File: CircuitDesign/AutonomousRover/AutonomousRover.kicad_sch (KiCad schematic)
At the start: 15 parts

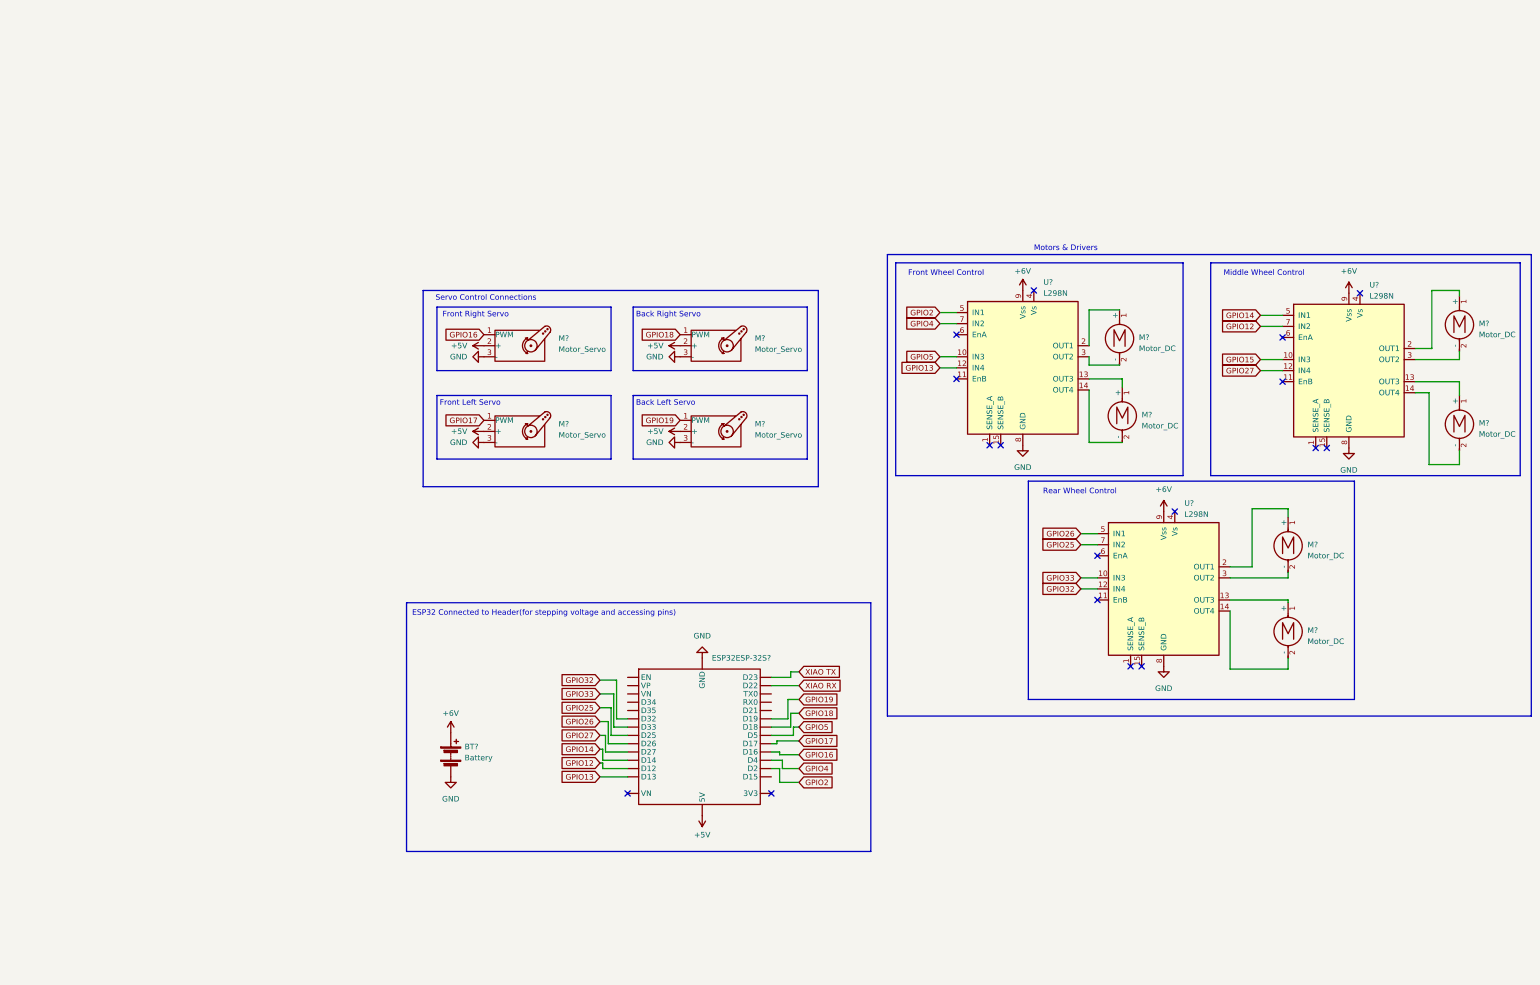
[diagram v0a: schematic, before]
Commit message: CAD, brief update, and circuit update
- Trailer CAD final
- Camera Holder CAD
- Brief update
- Circuit schematic update
- Fixed turning
- Log reasoning for full_stop from camera
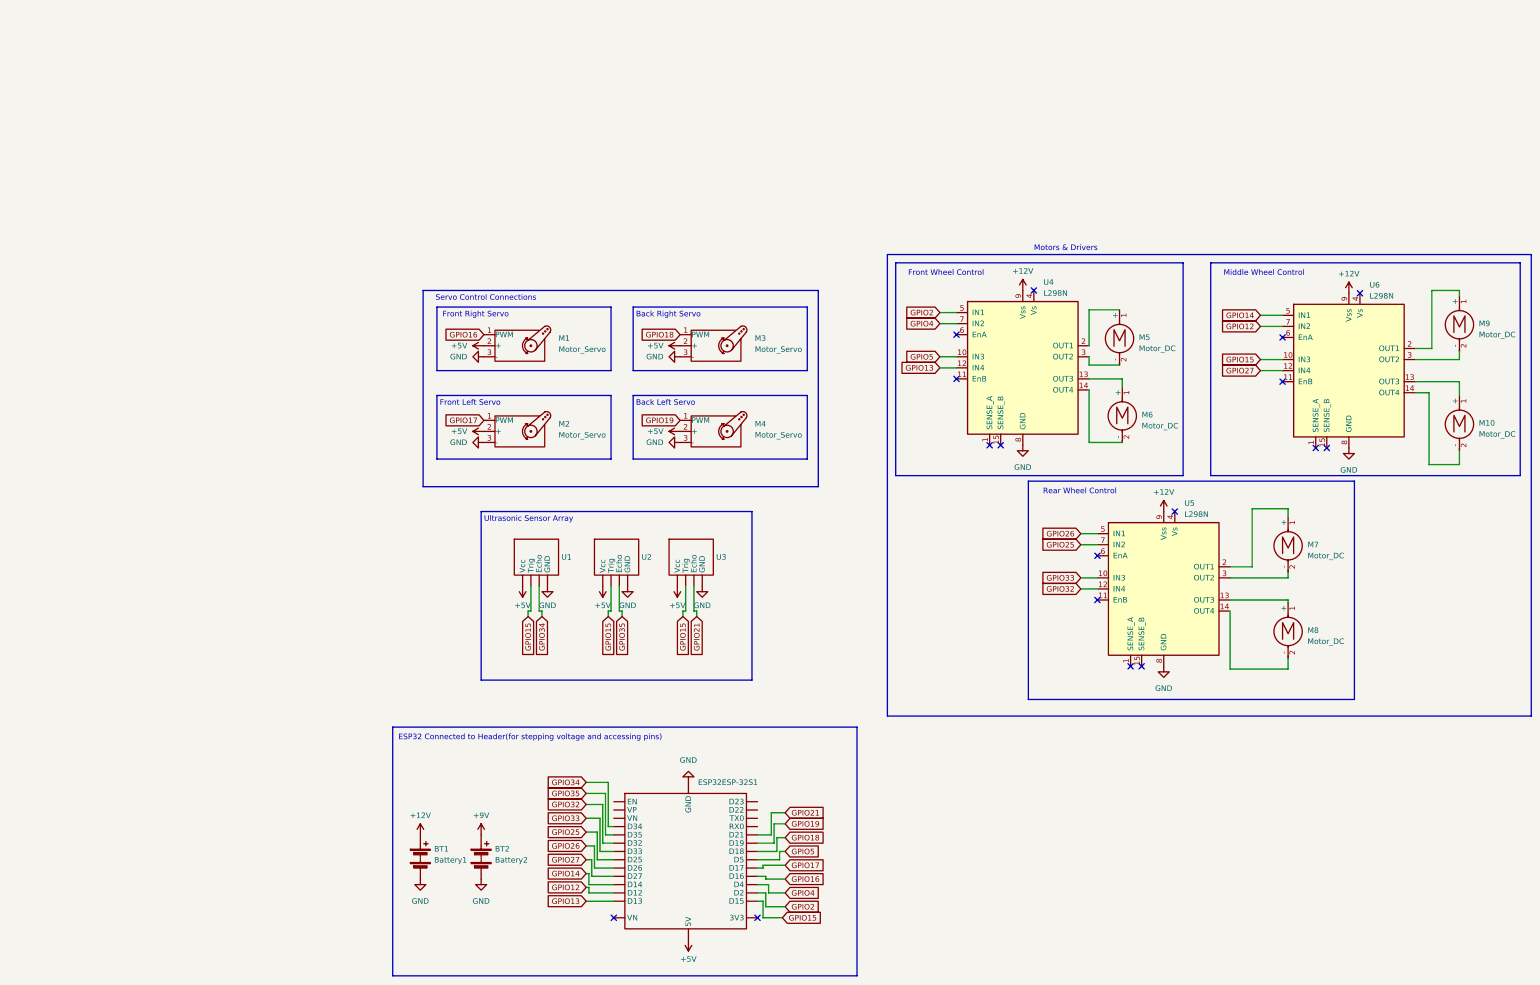
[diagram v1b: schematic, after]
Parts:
- added BT2: Battery2, symbol Device:Battery
- added U1, U2, U3: ~, symbol CustomSymbols:HC-SR04
- BT1: renamed from BT?; value Battery -> Battery1
- gave numbers to parts that had none: 14
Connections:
- net XIAO RX is gone; now on net GPIO5: ESP32ESP-32S1. (VP)
- net XIAO TX is gone; now on net GPIO5: ESP32ESP-32S1. (VP)
- net +5V: now also U1. (Vcc), U2. (Vcc), U3. (Vcc)
- net GND: now also BT2.2 (-), U1. (Vcc), U2. (Vcc), U3. (Vcc)
- net GPIO15: now also ESP32ESP-32S1. (VP), U1. (Vcc), U2. (Vcc), U3. (Vcc)
- net +6V renamed +12V
- new net +9V: BT2.1 (+)
- new net GPIO21: ESP32ESP-32S1. (VP), U3. (Vcc)
- new net GPIO34: ESP32ESP-32S1. (VP), U1. (Vcc)
- new net GPIO35: ESP32ESP-32S1. (VP), U2. (Vcc)
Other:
- note added: "Ultrasonic Sensor Array"
- moved on the sheet: BT1, ESP32ESP-32S1

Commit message: Updates to controller, server, and rover driver code
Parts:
- removed U2, U3: ~, symbol CustomSymbols:HC-SR04
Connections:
- net GPIO21 is gone; now on net GPIO5: ESP32ESP-32S1. (VP)
- net GPIO35 is gone; now on net GPIO5: ESP32ESP-32S1. (VP)
- no-connect marks 17 -> 28
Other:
- note added: "Ultrasonic Sensor"
- note removed: "Ultrasonic Sensor Array"

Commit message: Updated wiring and started TOF integration
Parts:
- removed U1: ~, symbol CustomSymbols:HC-SR04
- added VL53L5CX1: ~, symbol CustomSymbols:VL53L5CX
- renumbered U4 to U1, U5 to U2, U6 to U3
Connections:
- net GPIO34 is gone; now on net GPIO5: ESP32ESP-32S1. (VP)
- net GND: now also VL53L5CX1. (VIN)
- new net +3.3V: ESP32ESP-32S1. (VP), VL53L5CX1. (VIN)
- new net GPIO21: ESP32ESP-32S1. (VP), VL53L5CX1. (VIN)
- new net GPIO22: ESP32ESP-32S1. (VP), VL53L5CX1. (VIN)
- no-connect marks 28 -> 26
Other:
- note added: "TOF Sensor"
- note removed: "Ultrasonic Sensor"

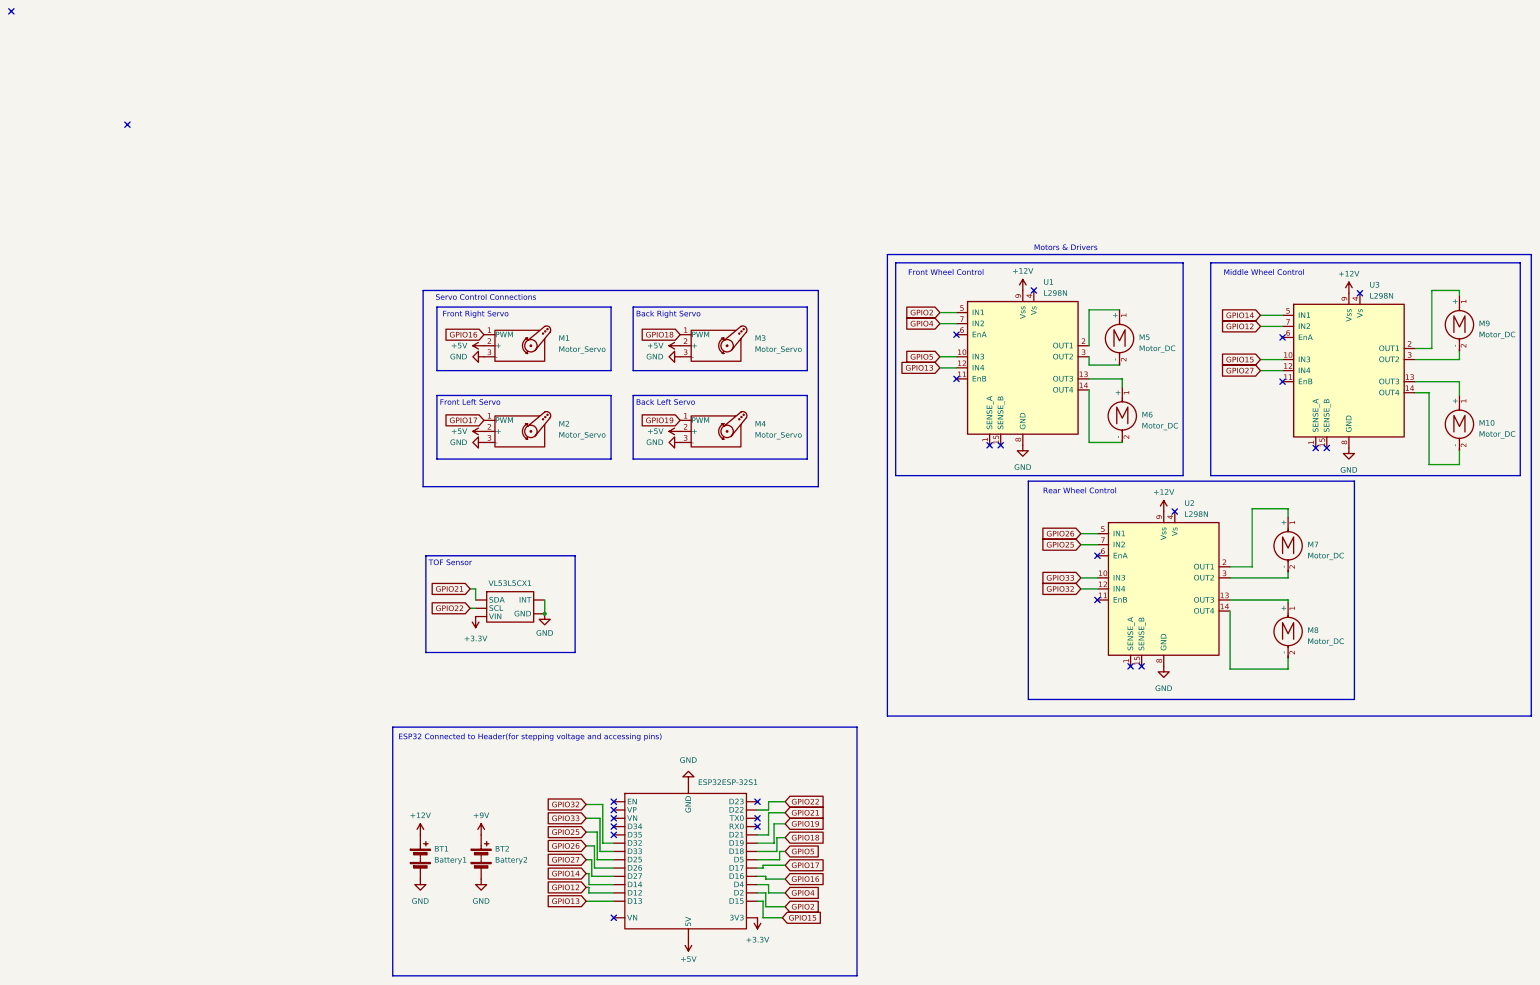
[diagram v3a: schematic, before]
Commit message: Directory clean up, removed servo, US Sensor. and middle motor code, and TOF sensor integration with OD
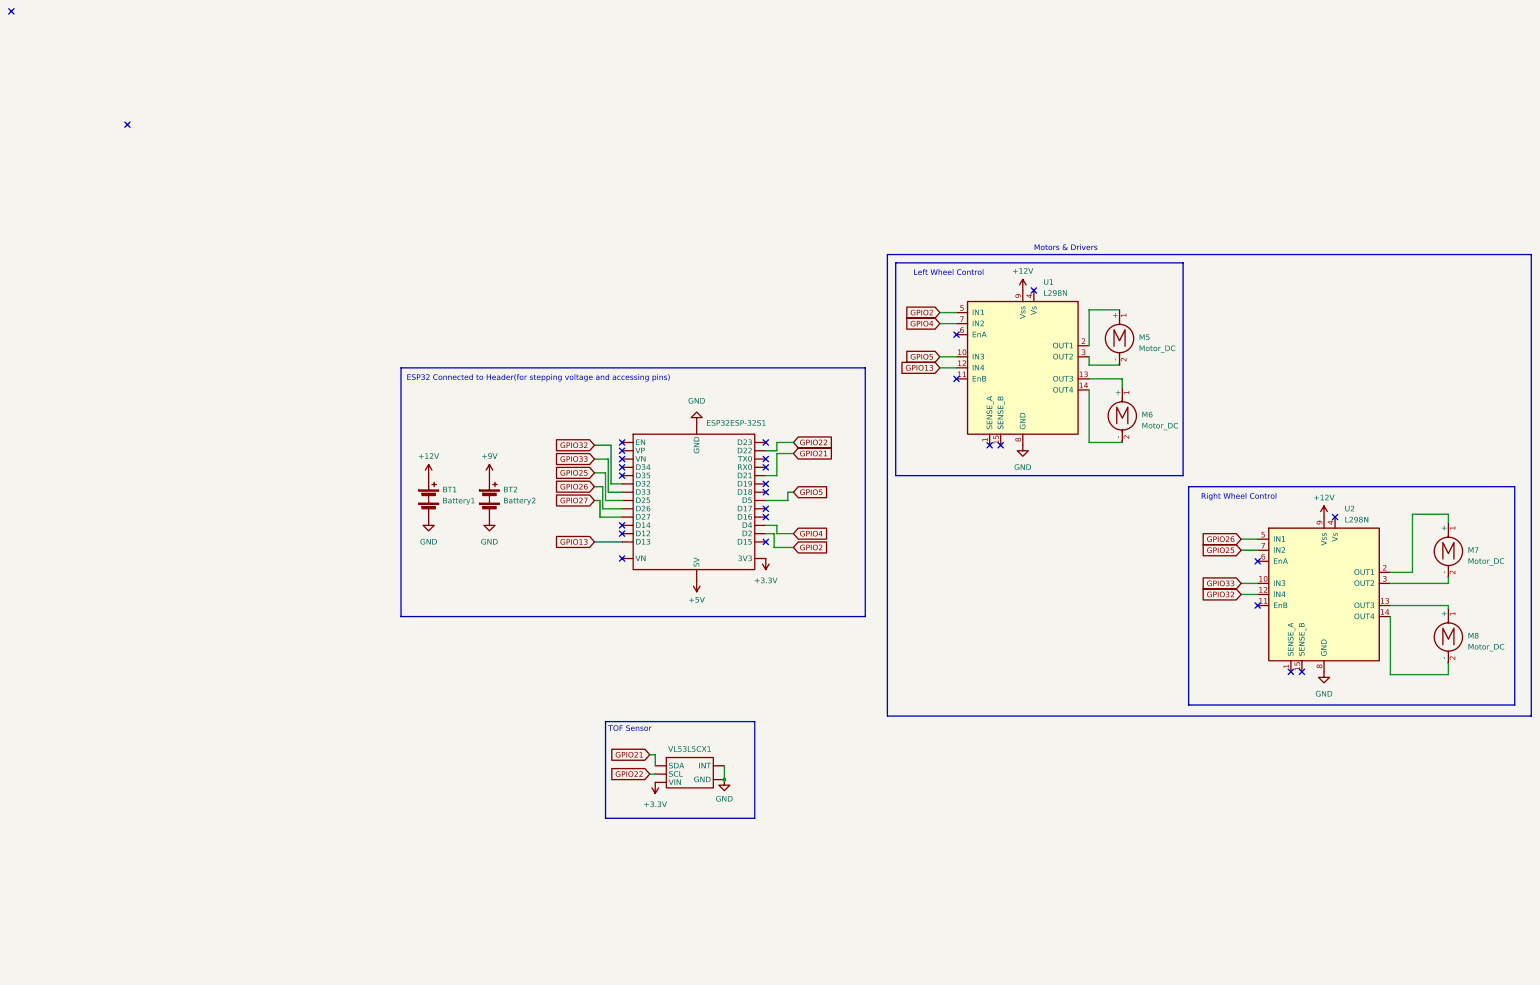
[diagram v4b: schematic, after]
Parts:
- removed M1, M2, M3, M4: Motor_Servo, symbol Motor:Motor_Servo
- removed M10, M9: Motor_DC, symbol Motor:Motor_DC
- removed U3: L298N, Package_TO_SOT_THT:TO-220-15_P2.54x2.54mm_StaggerOdd_Lead4.58mm_Vertical, symbol Driver_Motor:L298N
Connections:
- net GPIO12 is gone; now on net GPIO5: ESP32ESP-32S1. (VP)
- net GPIO14 is gone; now on net GPIO5: ESP32ESP-32S1. (VP)
- net GPIO15 is gone; now on net GPIO5: ESP32ESP-32S1. (VP)
- net GPIO16 is gone; now on net GPIO5: ESP32ESP-32S1. (VP)
- net GPIO17 is gone; now on net GPIO5: ESP32ESP-32S1. (VP)
- net GPIO18 is gone; now on net GPIO5: ESP32ESP-32S1. (VP)
- net GPIO19 is gone; now on net GPIO5: ESP32ESP-32S1. (VP)
- no-connect marks 26 -> 28
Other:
- note added: "Left Wheel Control"
- note added: "Right Wheel Control"
- note removed: "Back Left Servo"
- note removed: "Back Right Servo"
- note removed: "Front Left Servo"
- note removed: "Front Right Servo"
- note removed: "Front Wheel Control"
- note removed: "Middle Wheel Control"
- note removed: "Rear Wheel Control"
- note removed: "Servo Control Connections"
- moved on the sheet: BT1, BT2, ESP32ESP-32S1, M7, M8, U2, VL53L5CX1
